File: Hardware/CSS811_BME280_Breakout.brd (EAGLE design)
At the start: 25.4 x 25.4 mm, 25 parts, among them J1 JST, J2 CCS811 Options, J3 JST, J4 PTH, U2 CCS811

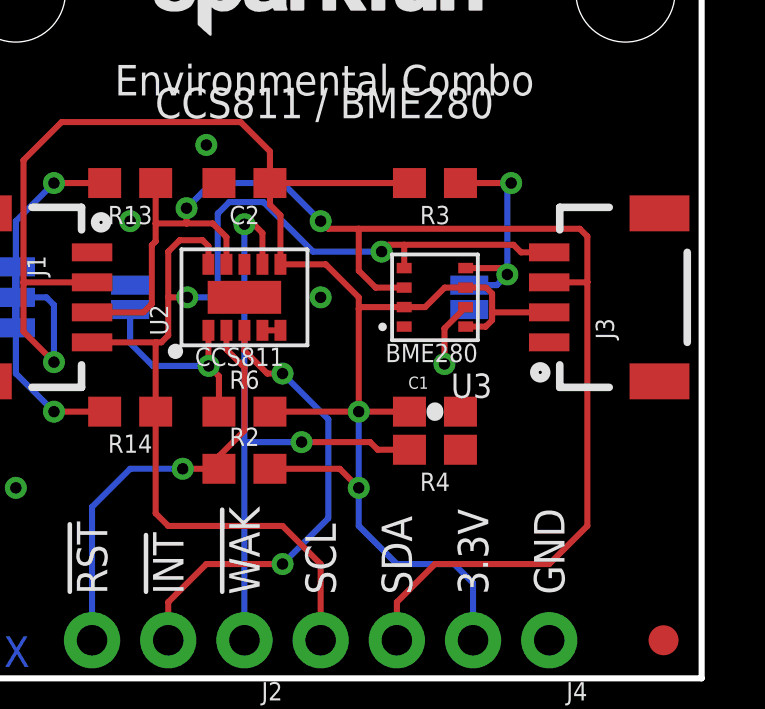
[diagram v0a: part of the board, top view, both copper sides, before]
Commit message: Updated parts to fit with SFE library
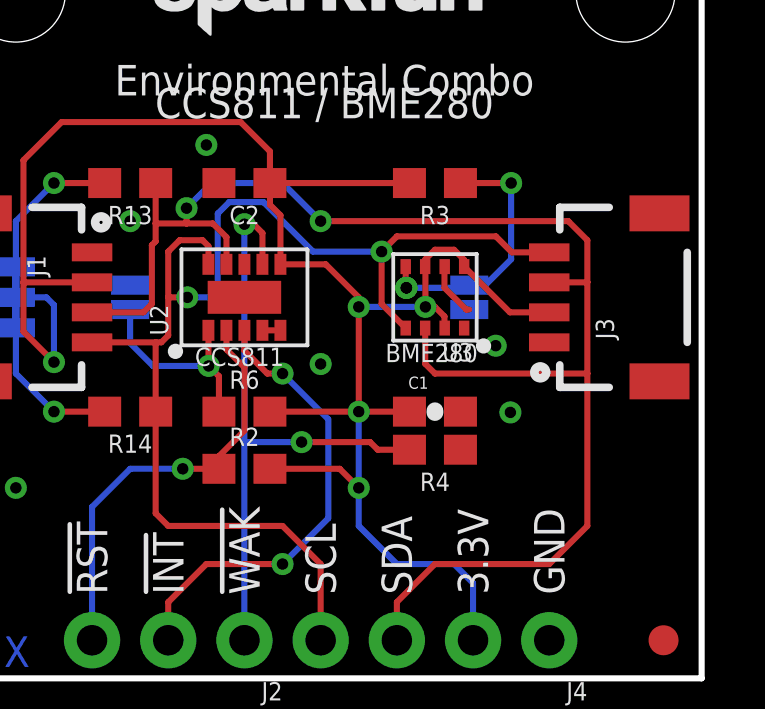
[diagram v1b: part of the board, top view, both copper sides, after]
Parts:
- J1, J3: value JST -> Qwiic Right Angle; device SparkX:1X04_1MM_RA -> SparkFun-Connectors:1X04_1MM_RA
- U2: device SparkX:LGA10 -> SparkFun-Sensors:LGA10
- U3: value (none) -> BME280; device SparkX:BME280_LGA -> SparkFun-Sensors:LGA-8-2.5X2.5
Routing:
- net SDA: track 47.3 -> 50.9 mm
- net SCL: track 39.2 -> 41.6 mm
- net 3.3V: track 64.1 -> 65.7 mm, vias 3 -> 5
- net SDO/ADR: track 7.68 -> 8.83 mm
- net GND: track 2.19 -> 1.84 mm, vias 5 -> 6

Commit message: Pre design review changes
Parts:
- added LOGO2: REVISION, SparkFun-Aesthetics:REVISION
- C1: device SparkFun-Capacitors:0603-CAP -> SparkFun-Capacitors:0603
- moved C1 2.84 mm to (19.1, 7.62), turned to 270 degrees
- turned R4 to 90 degrees
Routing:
- net 3.3V: track 65.7 -> 70.8 mm
- net SDO/ADR: track 8.83 -> 11.2 mm
- net !WAKE: track 21.5 -> 23.6 mm
- net SCL: track 41.6 -> 43.7 mm
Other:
- board text added: "V01"
- board text removed: "X11"

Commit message: Added Dimensions
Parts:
- removed U$1: (no value), SparkFun-Aesthetics:SFE_LOGO_NAME_.1
- LOGO1: value SFE_LOGO_NAME_FLAME.1_INCH -> SFE_LOGO_NAME.1_INCH; device SparkFun-Aesthetics:SFE_LOGO_NAME_FLAME_.1 -> SparkFun-Aesthetics:SFE_LOGO_NAME_.1
- moved LOGO1 64.6 mm to (6.73, 21.2)
- moved LOGO2 33.9 mm to (-2.54, -24.1)
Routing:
- net 3.3V: track 70.8 -> 73.4 mm
- net NTC_SENSE: track 0.60 -> 1.97 mm
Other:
- board text added: "Andrew England"

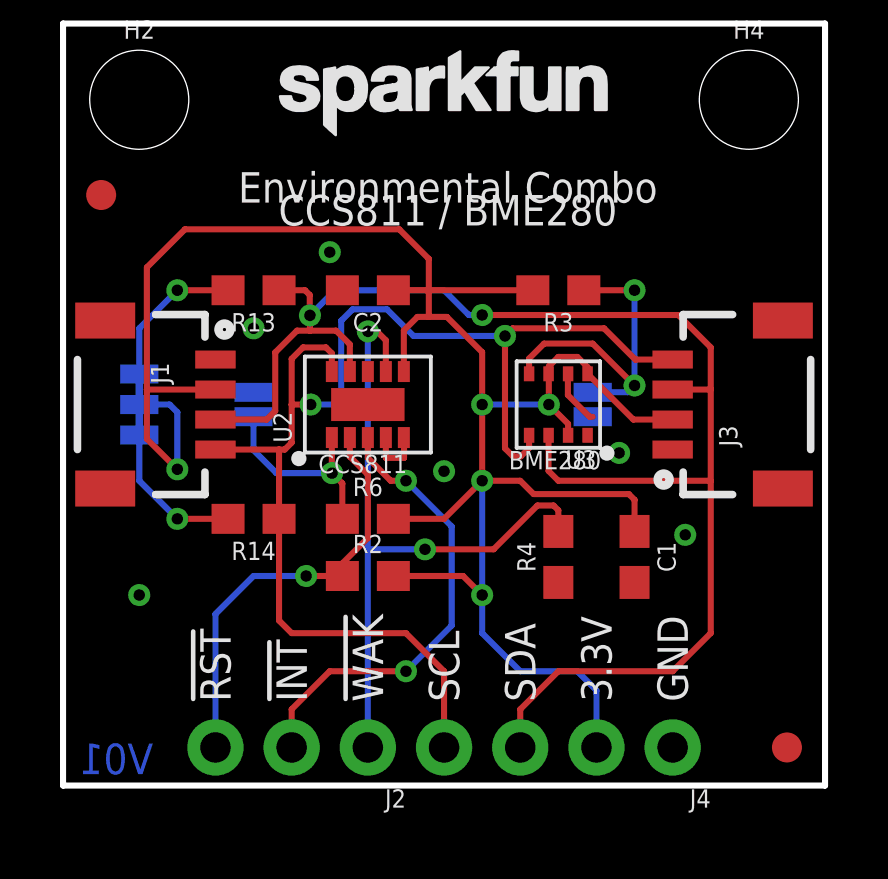
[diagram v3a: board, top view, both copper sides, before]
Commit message: Added fiducials to bottom of board
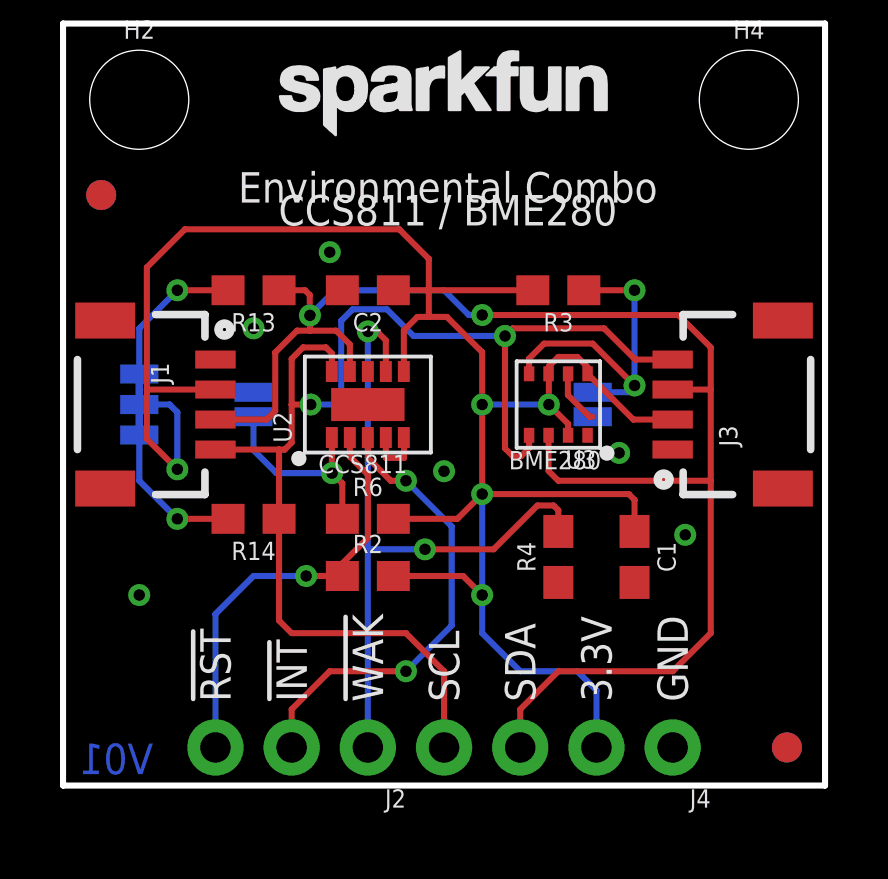
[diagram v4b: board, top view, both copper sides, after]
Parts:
- added FD3, FD4: FIDUCIAL1X2, SparkFun-Aesthetics:FIDUCIAL-1X2
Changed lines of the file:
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@@
 <grid distance="0.05" unitdist="inch" unit="inch" style="lines" multiple="1" display="yes" altdistance="0.00125" altunitdist="inch" altunit="inch"/>
 <layers>
-<layer number="1" name="Top" color="4" fill="1" visible="yes" active="yes"/>
+<layer number="1" name="Top" color="4" fill="1" visible="no" active="yes"/>
 <layer number="2" name="Route2" color="1" fill="3" visible="no" active="no"/>
 <layer number="3" name="Route3" color="4" fill="3" visible="no" active="no"/>
@@
 <layer number="23" name="tOrigins" color="15" fill="1" visible="yes" active="yes"/>
 <layer number="24" name="bOrigins" color="15" fill="1" visible="yes" active="yes"/>
-<layer number="25" name="tNames" color="7" fill="1" visible="yes" active="yes"/>
-<layer number="26" name="bNames" color="7" fill="1" visible="yes" active="yes"/>
-<layer number="27" name="tValues" color="7" fill="1" visible="yes" active="yes"/>
-<layer number="28" name="bValues" color="7" fill="1" visible="yes" active="yes"/>
-<layer number="29" name="tStop" color="7" fill="3" visible="no" active="yes"/>
+<layer number="25" name="tNames" color="7" fill="1" visible="no" active="yes"/>
+<layer number="26" name="bNames" color="7" fill="1" visible="no" active="yes"/>
+<layer number="27" name="tValues" color="7" fill="1" visible="no" active="yes"/>
+<layer number="28" name="bValues" color="7" fill="1" visible="no" active="yes"/>
+<layer number="29" name="tStop" color="7" fill="3" visible="yes" active="yes"/>
 <layer number="30" name="bStop" color="7" fill="6" visible="no" active="yes"/>
-<layer number="31" name="tCream" color="7" fill="4" visible="no" active="yes"/>
+<layer number="31" name="tCream" color="7" fill="4" visible="yes" active="yes"/>
 <layer number="32" name="bCream" color="7" fill="5" visible="no" active="yes"/>
 <layer number="33" name="tFinish" color="6" fill="3" visible="no" active="yes"/>
@@
 <element name="LOGO2" library="SparkFun-Aesthetics" package="REVISION" value="REVISION" x="-2.54" y="-24.13"/>
 <element name="LOGO1" library="SparkFun-Aesthetics" package="SFE_LOGO_NAME_.1" value="SFE_LOGO_NAME.1_INCH" x="6.731" y="21.17725"/>
+<element name="FD3" library="SparkFun-Aesthetics" package="FIDUCIAL-1X2" value="FIDUCIAL1X2" x="24.13" y="1.27" rot="MR0"/>
+<element name="FD4" library="SparkFun-Aesthetics" package="FIDUCIAL-1X2" value="FIDUCIAL1X2" x="1.27" y="19.685" rot="MR0"/>
 </elements>
 <signals>
@@
 <wire x1="2.794" y1="13.2" x2="5.08" y2="13.2" width="0.2032" layer="1"/>
 <wire x1="15.66" y1="16.51" x2="12.22375" y2="16.51" width="0.2032" layer="1"/>
-<via x="13.97" y="10.16" extent="1-16" drill="0.381"/>
+<via x="13.97" y="9.7155" extent="1-16" drill="0.381"/>
 <wire x1="12.22375" y1="16.51" x2="12.1285" y2="16.51" width="0.2032" layer="1"/>
 <wire x1="12.1285" y1="16.51" x2="11.01" y2="16.51" width="0.2032" layer="1"/>
-<wire x1="13.97" y1="6.35" x2="13.97" y2="10.16" width="0.2032" layer="16"/>
+<wire x1="13.97" y1="6.35" x2="13.97" y2="9.7155" width="0.2032" layer="16"/>
 <wire x1="17.145" y1="3.81" x2="17.78" y2="3.175" width="0.2032" layer="16"/>
 <wire x1="17.78" y1="3.175" x2="17.78" y2="1.27" width="0.2032" layer="16"/>
@@
 <wire x1="16.185" y1="13.725" x2="16.1925" y2="13.7175" width="0.2032" layer="1"/>
 <wire x1="16.1925" y1="13.7175" x2="16.1925" y2="12.7" width="0.2032" layer="1"/>
-<wire x1="13.97" y1="12.7" x2="13.97" y2="10.16" width="0.2032" layer="1"/>
+<wire x1="13.97" y1="12.7" x2="13.97" y2="9.7155" width="0.2032" layer="1"/>
 <wire x1="13.97" y1="12.7" x2="16.1925" y2="12.7" width="0.2032" layer="16"/>
 <wire x1="16.1925" y1="12.7" x2="16.835" y2="12.0575" width="0.2032" layer="1"/>
 <wire x1="16.835" y1="12.0575" x2="16.835" y2="11.675" width="0.2032" layer="1"/>
-<wire x1="13.97" y1="10.16" x2="12.7" y2="8.89" width="0.2032" layer="1"/>
-<wire x1="12.7" y1="8.89" x2="11.01" y2="8.89" width="0.2032" layer="1"/>
+<wire x1="13.1445" y1="8.89" x2="11.01" y2="8.89" width="0.2032" layer="1"/>
 <wire x1="19.05" y1="8.47" x2="19.05" y2="9.525" width="0.2032" layer="1"/>
 <wire x1="19.05" y1="9.525" x2="18.8595" y2="9.7155" width="0.2032" layer="1"/>
-<wire x1="18.8595" y1="9.7155" x2="15.6845" y2="9.7155" width="0.2032" layer="1"/>
-<wire x1="15.6845" y1="9.7155" x2="15.24" y2="10.16" width="0.2032" layer="1"/>
-<wire x1="15.24" y1="10.16" x2="13.97" y2="10.16" width="0.2032" layer="1"/>
+<wire x1="18.8595" y1="9.7155" x2="13.97" y2="9.7155" width="0.2032" layer="1"/>
 <wire x1="3.556" y1="12.7" x2="2.54" y2="12.7" width="0.2032" layer="16"/>
 <wire x1="11.36" y1="13.8" x2="11.36" y2="15.17" width="0.2032" layer="1"/>
@@
 <wire x1="13.97" y1="14.44625" x2="12.79525" y2="15.621" width="0.2032" layer="1"/>
 <wire x1="12.79525" y1="15.621" x2="12.192" y2="15.621" width="0.2032" layer="1"/>
+<wire x1="13.97" y1="9.7155" x2="13.1445" y2="8.89" width="0.2032" layer="1"/>
 </signal>
 <signal name="!RST">

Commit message: Post design review aesthetic changes
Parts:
- added LOGO3: SFE_LOGO_NAME.1_INCH, SparkFun-Aesthetics:SFE_LOGO_NAME_.1
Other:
- board text added: "BME280 / CCS811"
- board text added: "Closed 0X5A"
- board text added: "Closed 0X76"
- board text added: "Open 0X5B"
- board text added: "Open 0X77"
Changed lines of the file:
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@@
 <text x="7.62" y="2.794" size="1.016" layer="22" font="vector" ratio="15" rot="MR90" align="center-left">!INT</text>
 <text x="5.08" y="2.794" size="1.016" layer="22" font="vector" ratio="15" rot="MR90" align="center-left">!RST</text>
-<text x="12.6238" y="19.177" size="1.2065" layer="22" font="vector" ratio="15" rot="MR0" align="center">CCS811 / BME280</text>
+<text x="12.6238" y="19.177" size="1.2065" layer="22" font="vector" ratio="15" rot="MR0" align="center">BME280 / CCS811</text>
 <text x="12.6238" y="19.939" size="1.016" layer="22" font="vector" ratio="15" rot="MR0" align="center">Environmental Combo
 </text>
@@
 <dimension x1="2.54" y1="22.86" x2="0" y2="22.86" x3="1.27" y3="26.67" textsize="1.778" layer="47"/>
 <dimension x1="22.86" y1="22.86" x2="0" y2="22.86" x3="11.43" y3="30.48" textsize="1.778" layer="47"/>
+<text x="18.9865" y="14.1605" size="0.8128" layer="22" font="vector" ratio="15" rot="MR0">Open
+0X77</text>
+<text x="17.78" y="10.16" size="0.8128" layer="22" font="vector" ratio="15" rot="MR0" align="center">Closed
+0X76</text>
+<text x="6.35" y="10.16" size="0.8128" layer="22" font="vector" ratio="15" rot="MR0" align="center">Closed
+0X5A</text>
+<text x="6.35" y="15.24" size="0.8128" layer="22" font="vector" ratio="15" rot="MR0" align="center">Open
+0X5B</text>
 </plain>
 <attributes>
@@
 <element name="FD3" library="SparkFun-Aesthetics" package="FIDUCIAL-1X2" value="FIDUCIAL1X2" x="24.13" y="1.27" rot="MR0"/>
 <element name="FD4" library="SparkFun-Aesthetics" package="FIDUCIAL-1X2" value="FIDUCIAL1X2" x="1.27" y="19.685" rot="MR0"/>
+<element name="LOGO3" library="SparkFun-Aesthetics" package="SFE_LOGO_NAME_.1" value="SFE_LOGO_NAME.1_INCH" x="18.669" y="21.17725" rot="MR0"/>
 </elements>
 <signals>

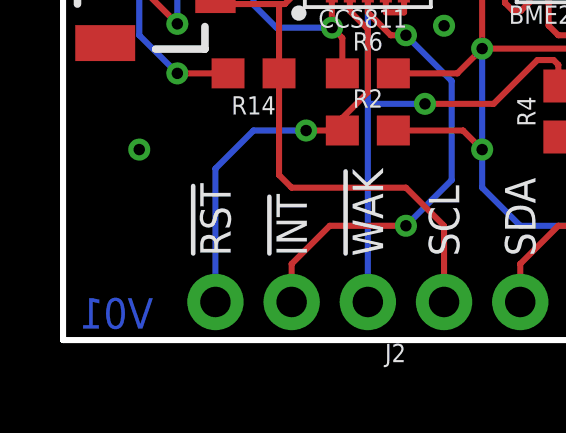
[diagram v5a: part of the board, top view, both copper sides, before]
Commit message: updated silk for Reds
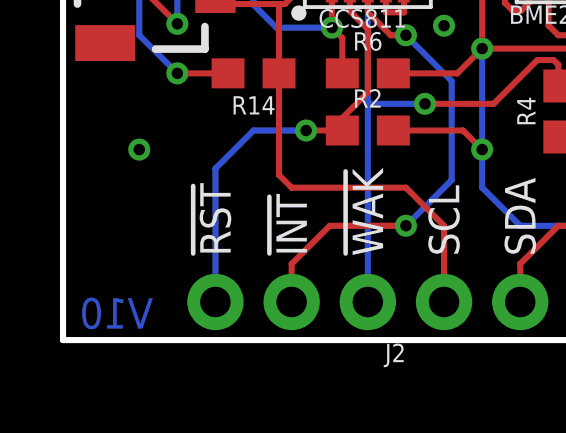
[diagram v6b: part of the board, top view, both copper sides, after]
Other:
- board text added: "V10"
- board text removed: "V01"
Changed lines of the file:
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@@
 <text x="20.32" y="2.794" size="1.016" layer="22" font="vector" ratio="15" rot="MR90" align="center-left">GND</text>
 <text x="12.827" y="19.177" size="1.016" layer="21" font="vector" ratio="15" align="center">CCS811 / BME280</text>
-<text x="1.778" y="0.889" size="1.016" layer="16" ratio="20" rot="MR180" align="center">V01</text>
+<text x="1.778" y="0.889" size="1.016" layer="16" ratio="20" rot="MR180" align="center">V10</text>
 <text x="4.572" y="12.827" size="0.889" layer="22" font="vector" ratio="15" rot="MR90" align="center">ADR1</text>
 <text x="16.51" y="-21.59" size="1.778" layer="51">Nathan Seidle</text>
